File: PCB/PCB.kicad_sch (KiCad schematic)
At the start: 28 parts, among them J1 sw, J2 sw, J3 detectors, J4 IR, SW1 SW_SPST, SW2 SW_SPST, SW3 SW_SPST, SW4 SW_SPST, U2 PC827, U3 24LC512, U4 24LC512, U5 24LC512, U6 24LC512

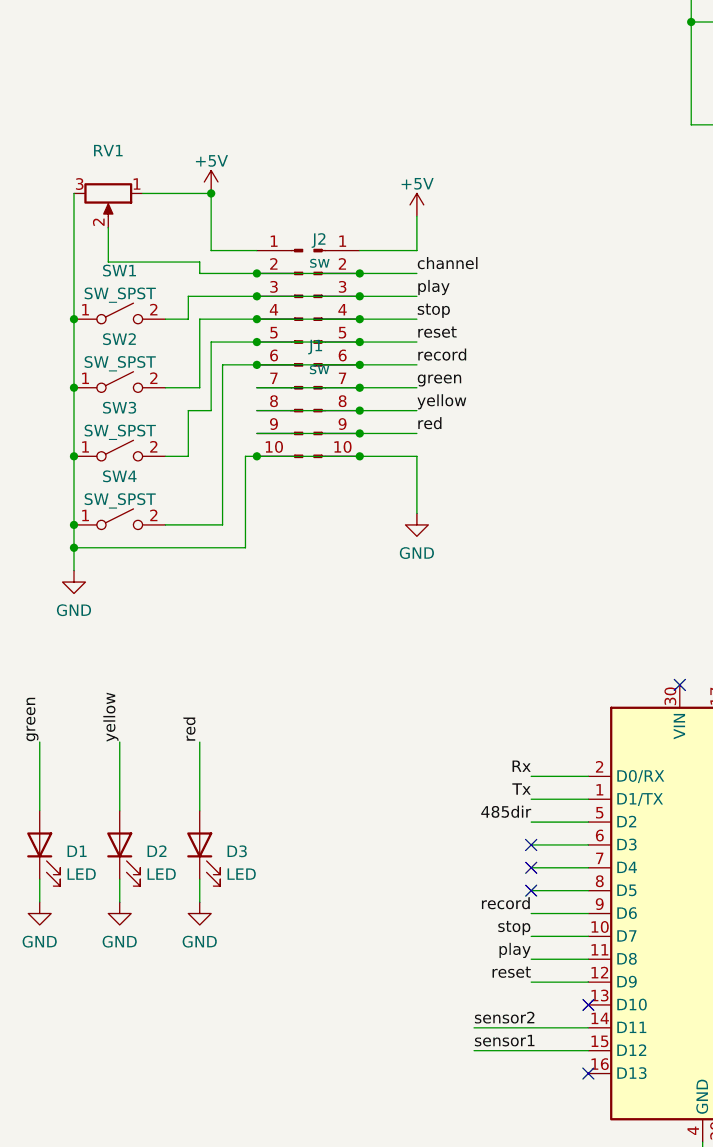
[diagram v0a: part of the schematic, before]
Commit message: did routing of PCB design. I must investigate if I want an extra I2C port to be used with I2C to create extra buttons to this system
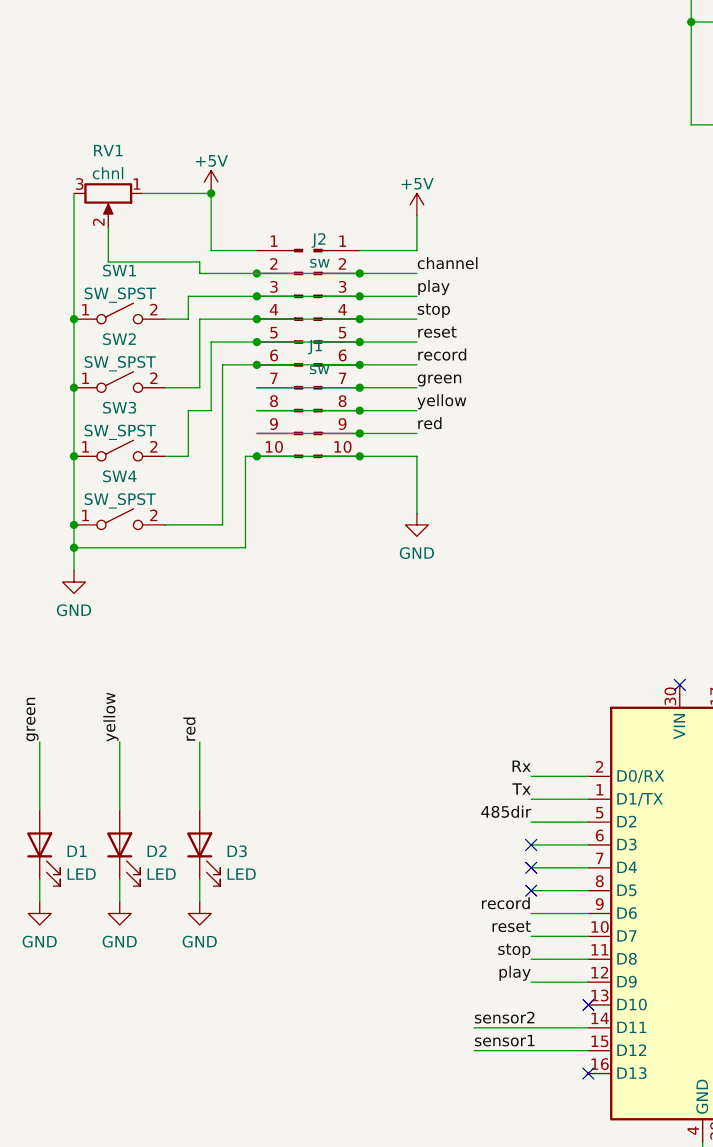
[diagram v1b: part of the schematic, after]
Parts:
- RV1: value (none) -> chnl
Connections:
- net play: now also A1.12 (D9); no longer A1.11 (D8)
- net reset: now also A1.10 (D7); no longer A1.12 (D9)
- net stop: now also A1.11 (D8); no longer A1.10 (D7)
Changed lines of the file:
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@@
     (effects (font (size 1.27 1.27)) (justify right bottom))
   )
-  (label "play" (at 76.2 142.24 180)
+  (label "play" (at 76.2 144.78 180)
     (effects (font (size 1.27 1.27)) (justify right bottom))
   )
@@
     (effects (font (size 1.27 1.27)) (justify right bottom))
   )
+  (label "reset" (at 76.2 139.7 180)
+    (effects (font (size 1.27 1.27)) (justify right bottom))
+  )
   (label "Tx" (at 76.2 124.46 180)
     (effects (font (size 1.27 1.27)) (justify right bottom))
@@
     (effects (font (size 1.27 1.27)) (justify left bottom))
   )
-  (label "reset" (at 76.2 144.78 180)
+  (label "stop" (at 76.2 142.24 180)
     (effects (font (size 1.27 1.27)) (justify right bottom))
   )
@@
   (label "stop" (at 63.5 71.12 0)
     (effects (font (size 1.27 1.27)) (justify left bottom))
-  )
-  (label "stop" (at 76.2 139.7 180)
-    (effects (font (size 1.27 1.27)) (justify right bottom))
   )
   (label "yellow" (at 63.5 81.28 0)
@@
     (in_bom yes) (on_board yes) (fields_autoplaced)
     (property "Reference" "RV1" (id 0) (at 29.21 52.4342 90))
-    (property "Value" "" (id 1) (at 29.21 54.9711 90))
+    (property "Value" "chnl" (id 1) (at 29.21 54.9711 90))
     (property "Footprint" "Connector_PinHeader_2.54mm:PinHeader_1x03_P2.54mm_Vertical" (id 2) (at 29.21 57.15 0)
       (effects (font (size 1.27 1.27)) hide)
@@
     (pin "7")
     (pin "8")
-    (pin "3")
-    (pin "4")
-    (pin "5")
-    (pin "6")
   )
   (symbol (lib_id "Connector:Conn_01x10_Male") (at 52.07 73.66 0) (unit 1)
@@
       (effects (font (size 1.27 1.27)) (justify left) hide)
     )
-    (pin "1")
-    (pin "2")
-    (pin "7")
-    (pin "8")
     (pin "3")
     (pin "4")

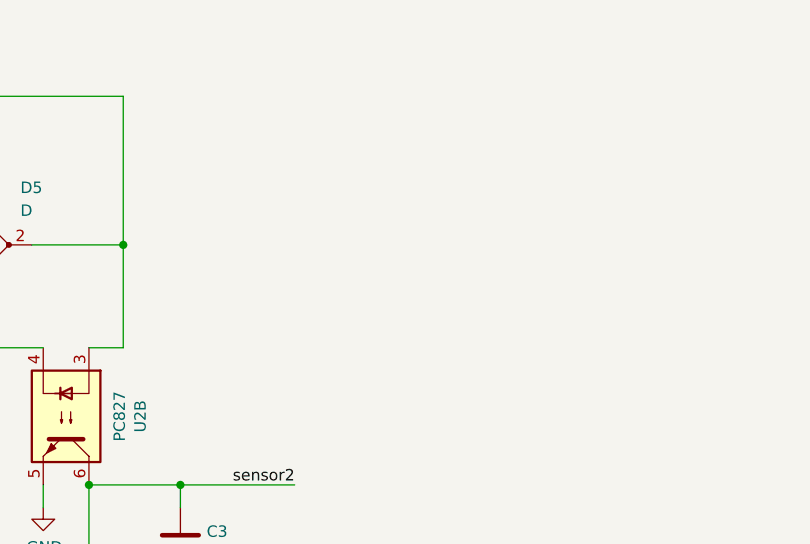
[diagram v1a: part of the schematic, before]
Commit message: added I2C connector on the side. Routing needs to be re done for a large part
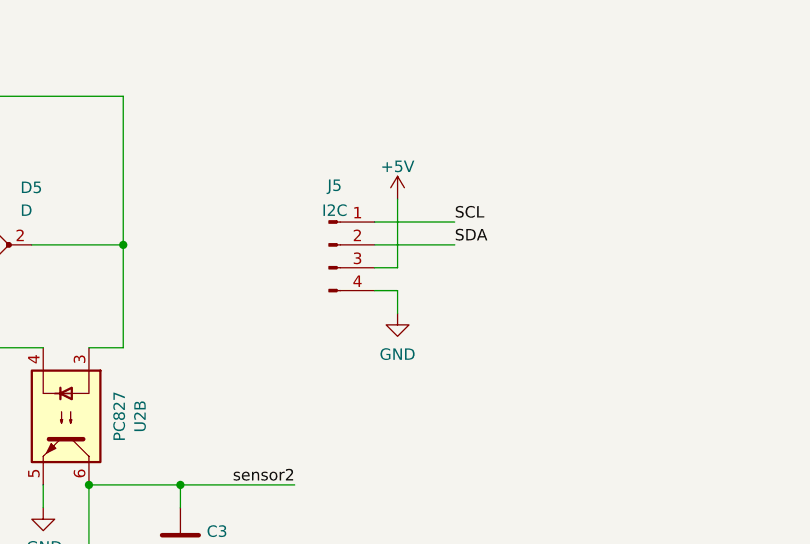
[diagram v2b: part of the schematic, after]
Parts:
- added J5: I2C, Connector_PinHeader_2.54mm:PinHeader_1x04_P2.54mm_Vertical, symbol Connector:Conn_01x04_Male
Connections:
- net +5V: now also J5.3 (Pin_3)
- net GND: now also J5.4 (Pin_4)
- net SCL: now also J5.1 (Pin_1)
- net SDA: now also J5.2 (Pin_2)
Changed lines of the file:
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@@
+    (stroke (width 0) (type default) (color 0 0 0 0))
+  )
+  (wire (pts (xy 182.88 40.64) (xy 182.88 33.02))
     (stroke (width 0) (type default) (color 0 0 0 0))
   )
@@
     (stroke (width 0) (type default) (color 0 0 0 0))
   )
+  (wire (pts (xy 180.34 38.1) (xy 189.23 38.1))
+    (stroke (width 0) (type default) (color 0 0 0 0))
+  )
+  (wire (pts (xy 182.88 43.18) (xy 182.88 45.72))
+    (stroke (width 0) (type default) (color 0 0 0 0))
+  )
   (wire (pts (xy 149.86 137.16) (xy 149.86 144.78))
     (stroke (width 0) (type default) (color 0 0 0 0))
@@
     (stroke (width 0) (type default) (color 0 0 0 0))
   )
+  (wire (pts (xy 180.34 40.64) (xy 182.88 40.64))
+    (stroke (width 0) (type default) (color 0 0 0 0))
+  )
   (wire (pts (xy 247.65 26.67) (xy 247.65 53.34))
     (stroke (width 0) (type default) (color 0 0 0 0))
@@
     (stroke (width 0) (type default) (color 0 0 0 0))
   )
+  (wire (pts (xy 180.34 43.18) (xy 182.88 43.18))
+    (stroke (width 0) (type default) (color 0 0 0 0))
+  )
   (wire (pts (xy 148.59 64.77) (xy 158.75 64.77))
     (stroke (width 0) (type default) (color 0 0 0 0))
@@
   )
   (wire (pts (xy 133.35 46.99) (xy 133.35 29.21))
+    (stroke (width 0) (type default) (color 0 0 0 0))
+  )
+  (wire (pts (xy 180.34 35.56) (xy 189.23 35.56))
     (stroke (width 0) (type default) (color 0 0 0 0))
   )
@@
     (effects (font (size 1.27 1.27)) (justify right bottom))
   )
+  (label "SDA" (at 189.23 38.1 0)
+    (effects (font (size 1.27 1.27)) (justify left bottom))
+  )
   (label "red" (at 39.37 118.11 90)
     (effects (font (size 1.27 1.27)) (justify left bottom))
@@
   )
   (label "green" (at 21.59 118.11 90)
+    (effects (font (size 1.27 1.27)) (justify left bottom))
+  )
+  (label "SCL" (at 189.23 35.56 0)
     (effects (font (size 1.27 1.27)) (justify left bottom))
   )
@@
     )
     (property "Datasheet" "" (id 3) (at 266.7 99.06 0)
+      (effects (font (size 1.27 1.27)) hide)
+    )
+    (pin "1")
+  )
+  (symbol (lib_id "power:+5V") (at 182.88 33.02 0) (unit 1)
+    (in_bom yes) (on_board yes) (fields_autoplaced)
+    (property "Reference" "#PWR0111" (id 0) (at 182.88 36.83 0)
+      (effects (font (size 1.27 1.27)) hide)
+    )
+    (property "Value" "+5V" (id 1) (at 182.88 29.4155 0))
+    (property "Footprint" "" (id 2) (at 182.88 33.02 0)
+      (effects (font (size 1.27 1.27)) hide)
+    )
+    (property "Datasheet" "" (id 3) (at 182.88 33.02 0)
+      (effects (font (size 1.27 1.27)) hide)
+    )
+    (pin "1")
+  )
+  (symbol (lib_id "power:GND") (at 182.88 45.72 0) (unit 1)
+    (in_bom yes) (on_board yes) (fields_autoplaced)
+    (property "Reference" "#PWR0110" (id 0) (at 182.88 52.07 0)
+      (effects (font (size 1.27 1.27)) hide)
+    )
+    (property "Value" "GND" (id 1) (at 182.88 50.2825 0))
+    (property "Footprint" "" (id 2) (at 182.88 45.72 0)
+      (effects (font (size 1.27 1.27)) hide)
+    )
+    (property "Datasheet" "" (id 3) (at 182.88 45.72 0)
       (effects (font (size 1.27 1.27)) hide)
     )
@@
     (pin "2")
   )
+  (symbol (lib_id "Connector:Conn_01x04_Male") (at 175.26 38.1 0) (unit 1)
+    (in_bom yes) (on_board yes) (fields_autoplaced)
+    (property "Reference" "J5" (id 0) (at 175.895 31.5173 0))
+    (property "Value" "I2C" (id 1) (at 175.895 34.2924 0))
+    (property "Footprint" "Connector_PinHeader_2.54mm:PinHeader_1x04_P2.54mm_Vertical" (id 2) (at 175.26 38.1 0)
+      (effects (font (size 1.27 1.27)) hide)
+    )
+    (property "Datasheet" "~" (id 3) (at 175.26 38.1 0)
+      (effects (font (size 1.27 1.27)) hide)
+    )
+    (pin "1")
+    (pin "2")
+    (pin "3")
+    (pin "4")
+  )
   (symbol (lib_id "power:GND") (at 143.51 67.31 0) (unit 1)
     (in_bom yes) (on_board yes)
@@
       (reference "#PWR0109") (unit 1) (value "GND") (footprint "")
     )
+    (path "/12728481-4f6b-4b9f-a3cf-5fe5a4933fca"
+      (reference "#PWR0110") (unit 1) (value "GND") (footprint "")
+    )
+    (path "/1204de68-3e17-4e41-94d9-3b7a17977a3c"
+      (reference "#PWR0111") (unit 1) (value "+5V") (footprint "")
+    )
     (path "/e163bc5e-146a-4fa5-8b35-c5afcf306ecc"
       (reference "#PWR0113") (unit 1) (value "GND") (footprint "")
@@
       (reference "J4") (unit 1) (value "IR") (footprint "Connector_PinHeader_2.54mm:PinHeader_2x03_P2.54mm_Vertical")
     )
+    (path "/e66cdece-4893-4be4-8985-52fc83792731"
+      (reference "J5") (unit 1) (value "I2C") (footprint "Connector_PinHeader_2.54mm:PinHeader_1x04_P2.54mm_Vertical")
+    )
     (path "/65b1fbaa-8a09-4983-8bd4-2ac52012db8d"
